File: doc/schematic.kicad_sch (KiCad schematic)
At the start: 12 parts, among them J1 USB connector, J2 TT04, J3 TT04

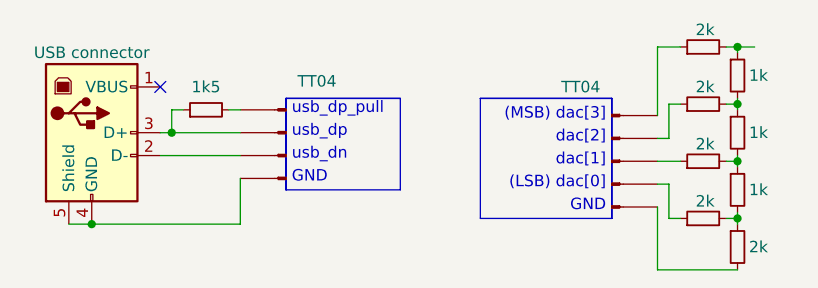
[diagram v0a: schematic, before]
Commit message: (doc) adding missing DAC schematic
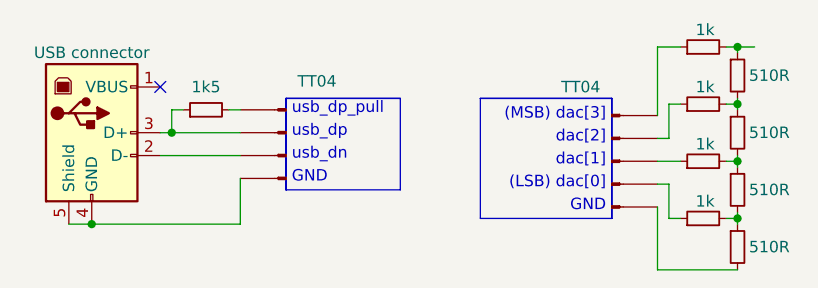
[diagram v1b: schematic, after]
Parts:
- R2: value 2k -> 510R
- R3, R4, R6, R7: value 2k -> 1k
- R5, R8, R9: value 1k -> 510R
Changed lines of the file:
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@@
       (effects (font (size 1.27 1.27)) (justify left) hide)
     )
-    (property "Value" "1k" (at 123.825 68.58 0)
+    (property "Value" "510R" (at 123.825 68.58 0)
       (effects (font (size 1.27 1.27)) (justify left))
     )
@@
       (effects (font (size 1.27 1.27)) (justify left) hide)
     )
-    (property "Value" "2k" (at 120.015 63.5 90)
+    (property "Value" "1k" (at 120.015 63.5 90)
       (effects (font (size 1.27 1.27)) (justify left))
     )
@@
       (effects (font (size 1.27 1.27)) (justify left) hide)
     )
-    (property "Value" "1k" (at 123.825 55.88 0)
+    (property "Value" "510R" (at 123.825 55.88 0)
       (effects (font (size 1.27 1.27)) (justify left))
     )
@@
       (effects (font (size 1.27 1.27)) (justify left) hide)
     )
-    (property "Value" "1k" (at 123.825 62.23 0)
+    (property "Value" "510R" (at 123.825 62.23 0)
       (effects (font (size 1.27 1.27)) (justify left))
     )
@@
       (effects (font (size 1.27 1.27)) (justify left) hide)
     )
-    (property "Value" "2k" (at 120.015 69.85 90)
+    (property "Value" "1k" (at 120.015 69.85 90)
       (effects (font (size 1.27 1.27)) (justify left))
     )
@@
       (effects (font (size 1.27 1.27)) (justify left) hide)
     )
-    (property "Value" "2k" (at 120.015 50.8 90)
+    (property "Value" "1k" (at 120.015 50.8 90)
       (effects (font (size 1.27 1.27)) (justify left))
     )
@@
       (effects (font (size 1.27 1.27)) (justify left) hide)
     )
-    (property "Value" "2k" (at 120.015 57.15 90)
+    (property "Value" "1k" (at 120.015 57.15 90)
       (effects (font (size 1.27 1.27)) (justify left))
     )
@@
       (effects (font (size 1.27 1.27)) (justify left) hide)
     )
-    (property "Value" "2k" (at 123.825 74.93 0)
-      (effects (font (size 1.27 1.27)) (justify left))
-    )
+    (property "Value" "510R" (at 123.825 74.93 0)
+      (effects (font (size 1.27 1.27)) (justify left))
+    )

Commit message: (doc) Converted images to PNG.
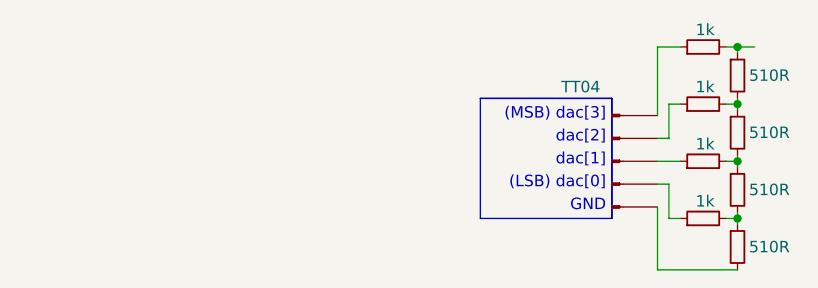
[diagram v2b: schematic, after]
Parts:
- removed J1: USB connector, symbol Connector:USB_B
- removed J2: TT04, symbol Connector:Conn_01x04_Pin
- removed R1: 1k5, symbol Device:R_Small
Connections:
- no-connect marks 1 -> 0
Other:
- note removed: "usb_dn"
- note removed: "usb_dp"
- note removed: "usb_dp_pull"
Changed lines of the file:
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@@
 (kicad_sch (version 20230121) (generator eeschema)
   (paper "A4")
-  (junction (at 59.69 62.23) (diameter 0) (color 0 0 0 0)
-  )
   (junction (at 122.555 59.055) (diameter 0) (color 0 0 0 0)
   )
-  (junction (at 50.8 72.39) (diameter 0) (color 0 0 0 0)
-  )
   (junction (at 122.555 65.405) (diameter 0) (color 0 0 0 0)
   )
@@
   (junction (at 122.555 71.755) (diameter 0) (color 0 0 0 0)
   )
-  (no_connect (at 58.42 57.15))
-  (wire (pts (xy 66.04 59.69) (xy 67.31 59.69))
-    (stroke (width 0) (type default))
-  )
   (wire (pts (xy 122.555 52.705) (xy 124.46 52.705))
     (stroke (width 0) (type default))
@@
     (stroke (width 0) (type default))
   )
-  (wire (pts (xy 59.69 59.69) (xy 59.69 62.23))
-    (stroke (width 0) (type default))
-  )
   (wire (pts (xy 113.665 77.47) (xy 122.555 77.47))
     (stroke (width 0) (type default))
   )
   (wire (pts (xy 114.935 67.945) (xy 114.935 71.755))
-    (stroke (width 0) (type default))
-  )
-  (wire (pts (xy 58.42 64.77) (xy 67.31 64.77))
     (stroke (width 0) (type default))
   )
@@
     (stroke (width 0) (type default))
   )
-  (polyline (pts (xy 72.39 58.42) (xy 85.09 58.42))
-    (stroke (width 0) (type default) (color 132 0 0 1))
-  )
   (wire (pts (xy 113.665 70.485) (xy 113.665 77.47))
     (stroke (width 0) (type default))
@@
     (stroke (width 0) (type default))
   )
-  (wire (pts (xy 67.31 67.31) (xy 67.31 72.39))
-    (stroke (width 0) (type default))
-  )
-  (wire (pts (xy 58.42 62.23) (xy 59.69 62.23))
-    (stroke (width 0) (type default))
-  )
-  (wire (pts (xy 60.96 59.69) (xy 59.69 59.69))
-    (stroke (width 0) (type default))
-  )
   (wire (pts (xy 121.285 59.055) (xy 122.555 59.055))
     (stroke (width 0) (type default))
-  )
-  (polyline (pts (xy 72.39 68.58) (xy 72.39 58.42))
-    (stroke (width 0) (type default) (color 132 0 0 1))
   )
   (polyline (pts (xy 108.585 71.755) (xy 108.585 58.42))
     (stroke (width 0) (type default) (color 132 0 0 1))
   )
-  (wire (pts (xy 48.26 72.39) (xy 50.8 72.39))
-    (stroke (width 0) (type default))
-  )
   (wire (pts (xy 122.555 52.705) (xy 122.555 53.34))
     (stroke (width 0) (type default))
@@
     (stroke (width 0) (type default))
   )
-  (wire (pts (xy 50.8 72.39) (xy 67.31 72.39))
-    (stroke (width 0) (type default))
-  )
   (wire (pts (xy 114.935 59.055) (xy 116.205 59.055))
     (stroke (width 0) (type default))
@@
   )
   (wire (pts (xy 122.555 64.77) (xy 122.555 65.405))
-    (stroke (width 0) (type default))
-  )
-  (wire (pts (xy 59.69 62.23) (xy 67.31 62.23))
     (stroke (width 0) (type default))
   )
@@
     (fill (type color) (color 255 255 194 1))
   )
-  (rectangle (start 72.39 58.42) (end 85.09 68.58)
-    (stroke (width 0.0001) (type default) (color 255 255 194 1))
-    (fill (type color) (color 255 255 194 1))
-  )
   (text "GND" (at 107.95 71.12 0)
     (effects (font (size 1.27 1.27)) (justify right bottom))
   )
-  (text "usb_dp_pull" (at 73.025 60.325 0)
-    (effects (font (size 1.27 1.27)) (justify left bottom))
-  )
   (text "dac[1]" (at 107.95 66.04 0)
     (effects (font (size 1.27 1.27)) (justify right bottom))
@@
     (effects (font (size 1.27 1.27)) (justify right bottom))
   )
-  (text "usb_dp" (at 73.025 62.865 0)
-    (effects (font (size 1.27 1.27)) (justify left bottom))
-  )
   (text "(LSB) dac[0]" (at 107.95 68.58 0)
     (effects (font (size 1.27 1.27)) (justify right bottom))
   )
-  (text "usb_dn" (at 73.025 65.405 0)
-    (effects (font (size 1.27 1.27)) (justify left bottom))
-  )
   (text "(MSB) dac[3]" (at 107.95 60.96 0)
     (effects (font (size 1.27 1.27)) (justify right bottom))
-  )
-  (text "GND" (at 73.025 67.945 0)
-    (effects (font (size 1.27 1.27)) (justify left bottom))
   )
   (netclass_flag "" (length 2.54) (shape round) (at 124.46 52.705 270)
@@
         )
       )
-    )
-  )
-  (symbol (lib_id "Connector:Conn_01x04_Pin") (at 72.39 62.23 0) (mirror y) (unit 1)
-    (in_bom yes) (on_board yes) (dnp no)
-    (property "Reference" "J2" (at 73.66 62.865 0)
-      (effects (font (size 1.27 1.27)) (justify right) hide)
-    )
-    (property "Value" "TT04" (at 73.66 56.515 0)
-      (effects (font (size 1.27 1.27)) (justify right))
-    )
-    (property "Footprint" "" (at 72.39 62.23 0)
-      (effects (font (size 1.27 1.27)) hide)
-    )
-    (property "Datasheet" "~" (at 72.39 62.23 0)
-      (effects (font (size 1.27 1.27)) hide)
-    )
-    (property "eshop" "" (at 72.39 62.23 0)
-      (effects (font (size 1.27 1.27)) hide)
-    )
-    (pin "1")
-    (pin "2")
-    (pin "3")
-    (pin "4")
-    (instances
-      (project "schematic"
-        (path "/c1ba07ca-4e46-42d2-9493-b4a5fc17661e"
-          (reference "J2") (unit 1)
-        )
-      )
-    )
-  )
-  (symbol (lib_id "Connector:USB_B") (at 50.8 62.23 0) (unit 1)
-    (in_bom yes) (on_board yes) (dnp no) (fields_autoplaced)
-    (property "Reference" "J1" (at 50.8 50.8 0)
-      (effects (font (size 1.27 1.27)) hide)
-    )
-    (property "Value" "USB connector" (at 50.8 53.34 0)
-      (effects (font (size 1.27 1.27)))
-    )
-    (property "Footprint" "" (at 54.61 63.5 0)
-      (effects (font (size 1.27 1.27)) hide)
-    )
-    (property "Datasheet" " ~" (at 54.61 63.5 0)
-      (effects (font (size 1.27 1.27)) hide)
-    )
-    (pin "1")
-    (pin "2")
-    (pin "3")
-    (pin "4")
-    (pin "5")
-    (instances
-      (project "schematic"
-        (path "/c1ba07ca-4e46-42d2-9493-b4a5fc17661e"
-          (reference "J1") (unit 1)
-        )
-      )
-    )
-  )
-  (symbol (lib_id "Device:R_Small") (at 63.5 59.69 90) (unit 1)
-    (in_bom yes) (on_board yes) (dnp no) (fields_autoplaced)
-    (property "Reference" "R1" (at 63.5 54.61 90)
-      (effects (font (size 1.27 1.27)) hide)
-    )
-    (property "Value" "1k5" (at 63.5 57.15 90)
-      (effects (font (size 1.27 1.27)))
-    )
-    (property "Footprint" "" (at 63.5 59.69 0)
-      (effects (font (size 1.27 1.27)) hide)
-    )
-    (property "Datasheet" "~" (at 63.5 59.69 0)
-      (effects (font (size 1.27 1.27)) hide)
-    )
-    (pin "1")
-    (pin "2")
-    (instances
-      (project "schematic"
-        (path "/c1ba07ca-4e46-42d2-9493-b4a5fc17661e"
-          (reference "R1") (unit 1)
-        )
-      )
